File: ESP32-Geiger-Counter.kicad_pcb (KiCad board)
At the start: 2 copper layers, 137 x 84 mm, 85 parts, among them J1 2s1p Lipo Battery Pack (8.4V-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, J2 USB_C_Receptacle_USB2.0_16P, J5 Conn_01x07, Q1 STN1HNK60, Q3 2N7002, Q4 AO3401A, Q5 MMBT3904, SW1 SW_SPDT, SW2 RESET, SW3 BOOT, U1 BQ25886RGE, U2 AP63203WU, U3 ESP32-S3-WROOM-1, U4 UCC27517DBVR, U5 USBLC6-2SC6, U6 SBM-20 Geiger Mueller Tube

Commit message: top gnd pour
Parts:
- moved R10 55.9 mm to (207.6, 297.1), turned to -90 degrees
- moved R11 50.1 mm to (208.4, 294.1), turned to 180 degrees
- moved C18 49.1 mm to (208.4, 291.0)
- moved C23 14.6 mm to (142.3, 250.6), turned to -90 degrees
- moved SW2 12.0 mm to (203.3, 249.0)
- moved R26 11.5 mm to (194.3, 243.9), turned to 0 degrees
- moved SW3 9.49 mm to (203.3, 259.4)
- moved R28 4.14 mm to (183.0, 297.4)
- moved R27 3.18 mm to (189.8, 240.8), turned to 0 degrees
- moved Q3 2.95 mm to (189.7, 243.9), turned to -90 degrees
- moved Q4 2.16 mm to (182.9, 294.0)
- moved R23 1.80 mm to (154.8, 244.0)
- moved R24 1.80 mm to (162.6, 239.7)
- moved C28 1.80 mm to (165.2, 243.9)
- moved C29 1.80 mm to (163.2, 243.9)
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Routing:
- net +3.3V: track 0.00 -> 149.1 mm, vias 0 -> 4
- net /OLED_RST: track 0.00 -> 76.2 mm, vias 0 -> 2
- net /OLED_MOSI: track 0.00 -> 75.7 mm, vias 0 -> 2
- net /OLED_SCK: track 0.00 -> 71.5 mm, vias 0 -> 2
- net /HV_PWM: track 2.67 -> 71.6 mm, vias 0 -> 4
- net /VBAT_SENSE: track 0.00 -> 35.2 mm, vias 0 -> 2
- net Net-(U3-EN): track 0.00 -> 30.9 mm
- net Net-(U6-K): track 0.00 -> 30.4 mm, vias 0 -> 2
- net /PIEZO: track 0.00 -> 28.3 mm, vias 0 -> 4
- net Net-(U3-IO0): track 2.80 -> 21.5 mm
- net Net-(BZ1--): track 9.40 -> 24.3 mm
- net /VSYS_SW: track 112.4 -> 103.6 mm
- net Net-(Q4-G): track 12.3 -> 8.97 mm, vias 2 -> 0
- net Net-(Q3-G): track 2.19 -> 5.25 mm
- net /BATT: track 18.7 -> 21.7 mm
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
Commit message: added name for larp
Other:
- board text added: "Avalanche32 by Aron Szucs"

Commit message: layout changes
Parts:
- renumbered SW3 to BOOT, SW2 to RESET
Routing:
- net /HV_SENSE: track 6.11 -> 134.3 mm, vias 0 -> 2
- net /OLED_CS: track 0.00 -> 85.8 mm, vias 0 -> 2
- net /OLED_DC: track 0.00 -> 81.5 mm, vias 0 -> 2
- net /PULSE: track 2.56 -> 12.1 mm, vias 0 -> 2
- net +3.3V: track 149.1 -> 157.5 mm, vias 4 -> 6
- net GND: track 9.33 -> 17.1 mm, vias 1 -> 269
- net Net-(U1-VSET): track 0.27 -> 1.69 mm
- net Net-(U1-~{PG}): track 4.98 -> 4.36 mm

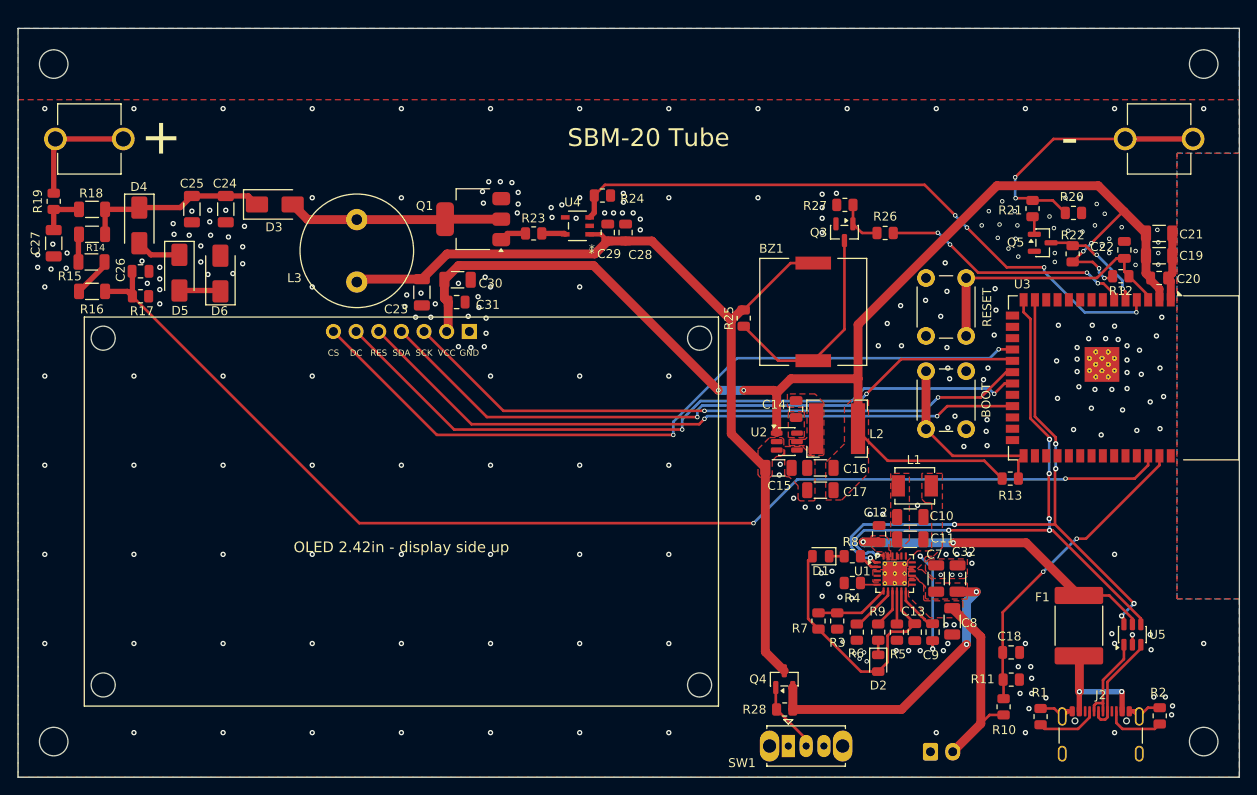
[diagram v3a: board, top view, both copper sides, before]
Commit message: fixed via stiching to look nice
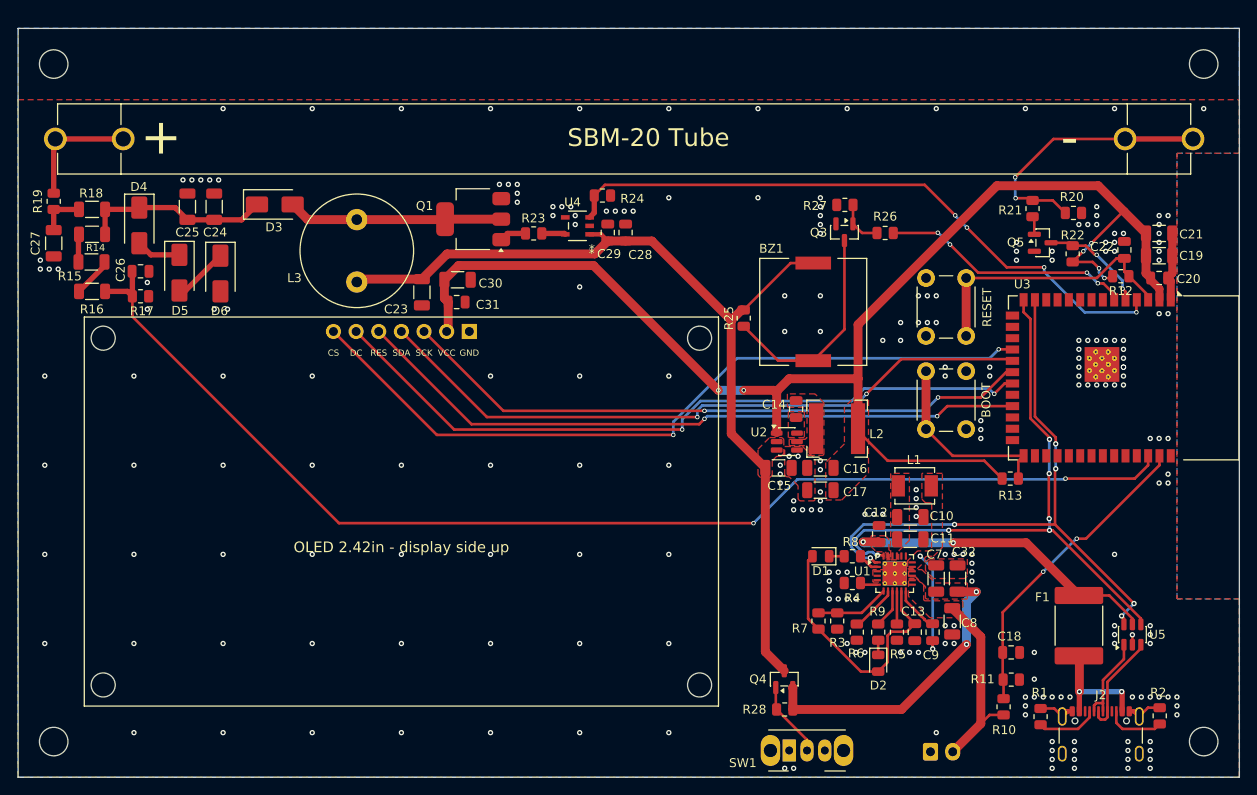
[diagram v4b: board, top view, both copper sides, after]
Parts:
- SW1: footprint Button_Switch_THT:SW_Slide_SPDT_Straight_CK_OS102011MS2Q -> Button_Switch_THT:SW_Slide_SPDT_Angled_CK_OS102011MA1Q
- moved C24 1.33 mm to (119.0, 241.0), turned to 90 degrees
- moved C25 0.57 mm to (116.0, 241.0), turned to 90 degrees
- moved SW1 0.51 mm to (183.5, 302.0)
- turned D6 to -90 degrees
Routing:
- net Net-(D5-A): track 4.64 -> 6.22 mm
- net /HV_SENSE: track 134.3 -> 135.7 mm
- net GND: track 17.1 -> 17.3 mm, vias 269 -> 250

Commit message: small changes
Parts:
- moved C23 0.63 mm to (142.5, 250.0)
- moved C31 0.31 mm to (146.2, 251.4)
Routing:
- net GND: vias 250 -> 280
